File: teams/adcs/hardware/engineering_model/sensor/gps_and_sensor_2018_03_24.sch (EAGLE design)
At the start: 50 parts, among them U1 LT1761-X, U2 LT1761-X, U3 OEM719, U4 LTC3624

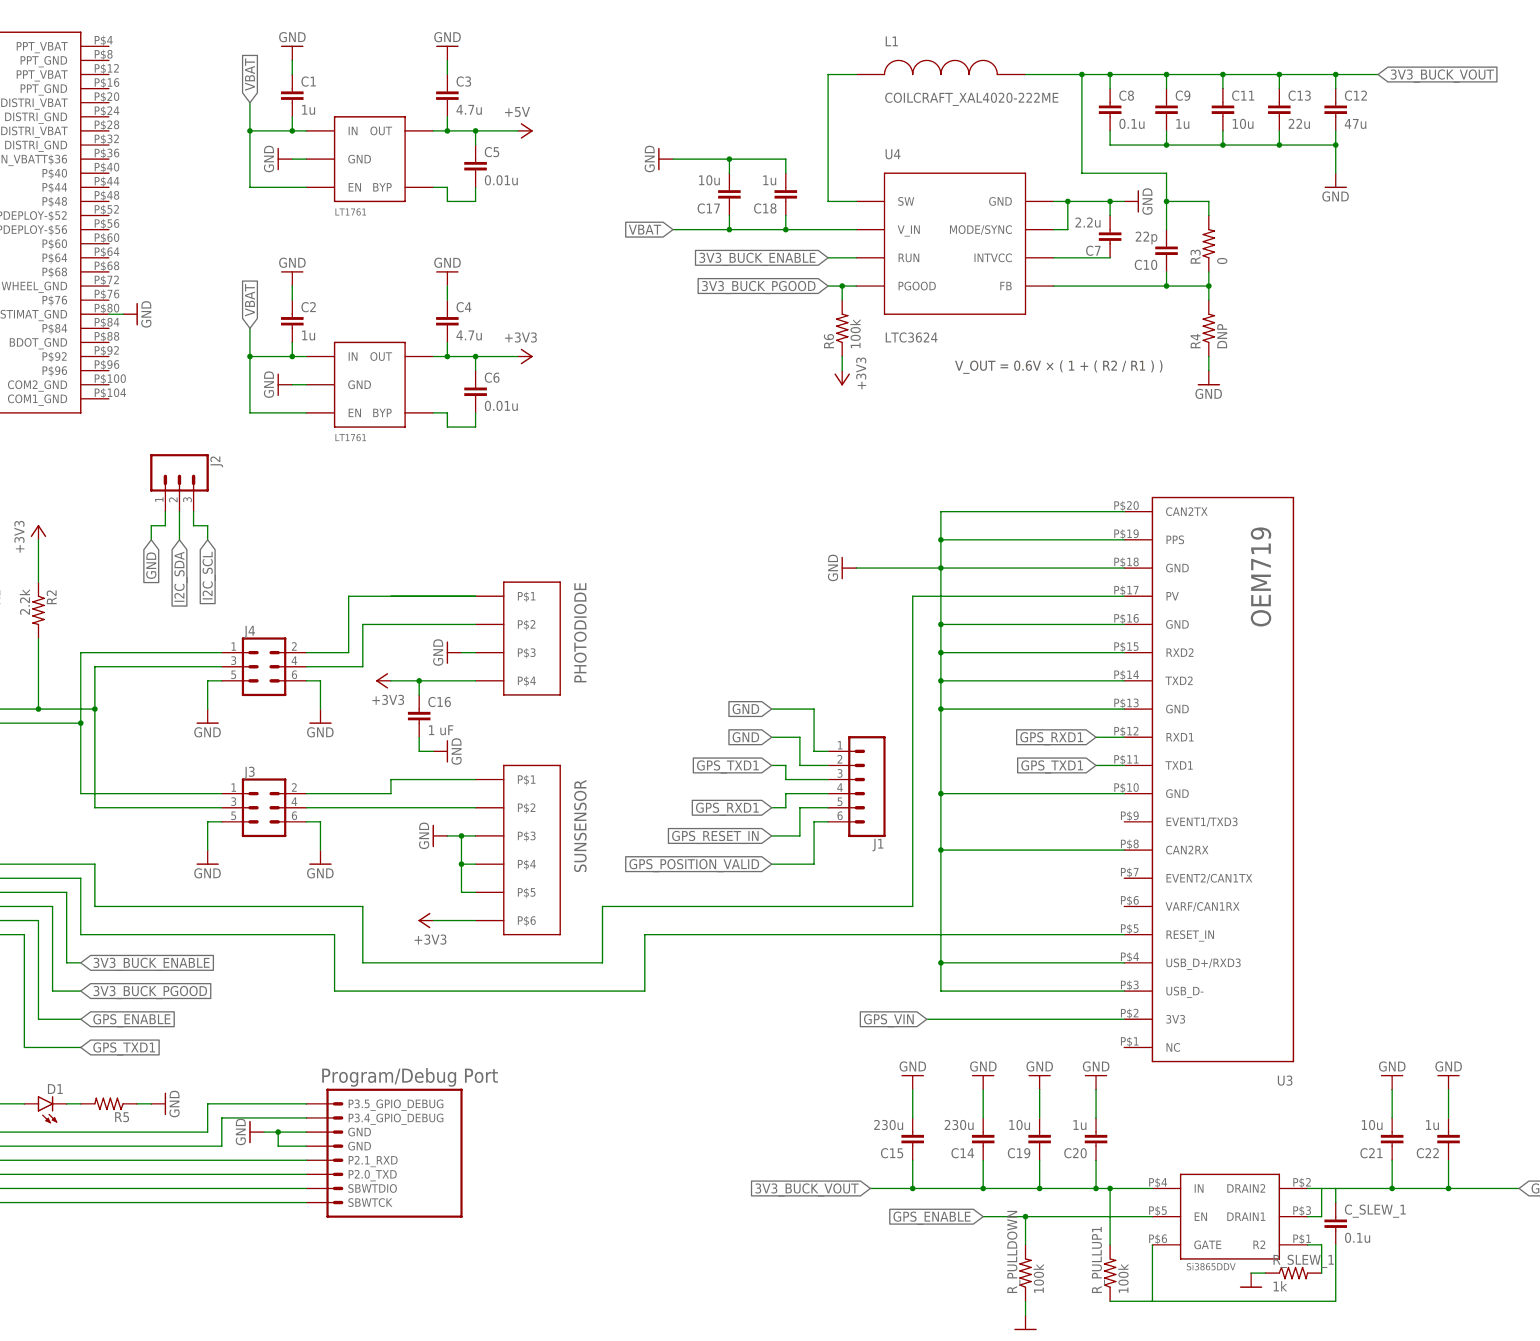
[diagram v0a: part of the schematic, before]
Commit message: ADCS/Sensor: Use picolock with more connectors and reformat component values
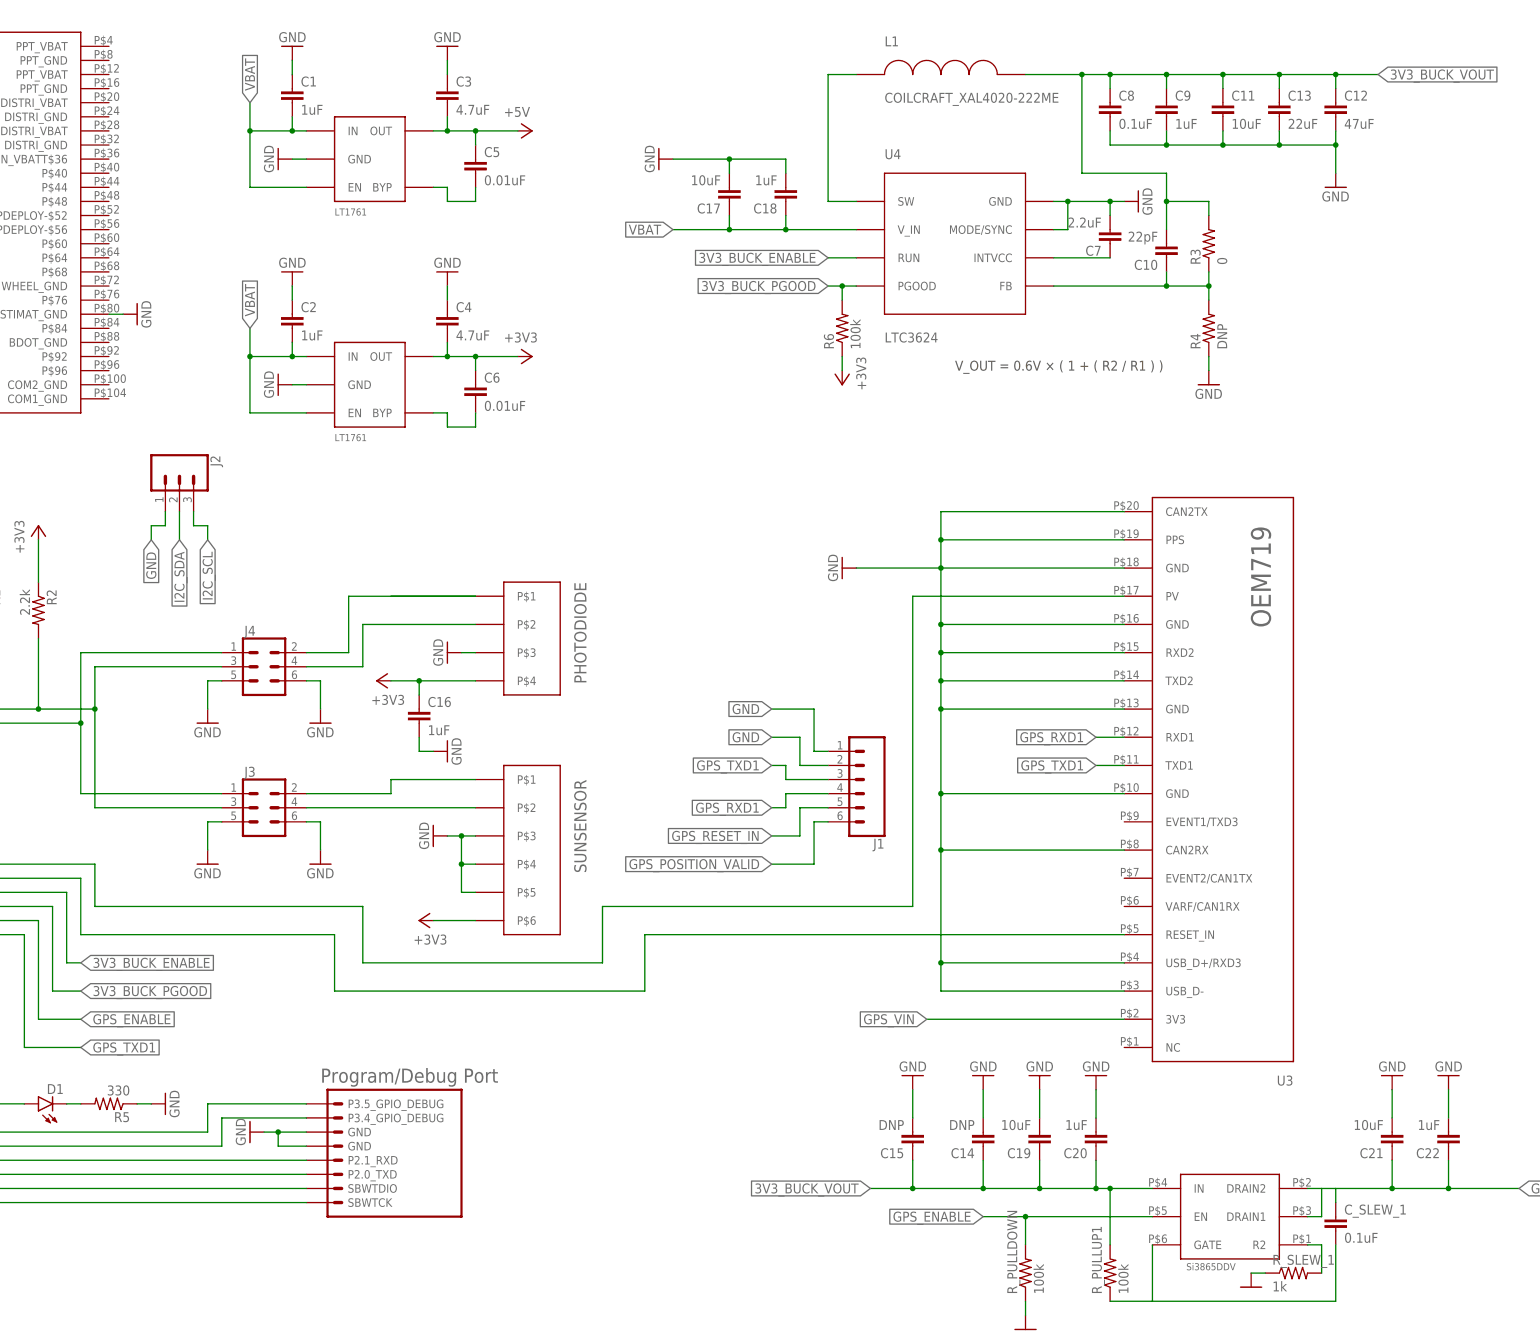
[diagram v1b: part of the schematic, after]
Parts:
- C1, C18, C2, C20, C22, C9: value 1u -> 1uF
- C10: value 22p -> 22pF
- C11, C17, C19, C21: value 10u -> 10uF
- C12: value 47u -> 47uF
- C13: value 22u -> 22uF
- C14, C15: value 230u -> DNP
- C16: value 1 uF -> 1uF
- C3, C4: value 4.7u -> 4.7uF
- C5, C6: value 0.01u -> 0.01uF
- C7: value 2.2u -> 2.2uF
- C8, C_SLEW_1: value 0.1u -> 0.1uF
- R5: value (none) -> 330
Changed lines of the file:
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@@
 <part name="GND7" library="supply1" library_urn="urn:adsk.eagle:library:371" deviceset="GND" device=""/>
 <part name="P+2" library="supply1" library_urn="urn:adsk.eagle:library:371" deviceset="+5V" device=""/>
-<part name="C5" library="DubSat1 Components" deviceset="CAPACITOR" device="0805" value="0.01u"/>
-<part name="C1" library="DubSat1 Components" deviceset="CAPACITOR" device="0805" value="1u"/>
+<part name="C5" library="DubSat1 Components" deviceset="CAPACITOR" device="0805" value="0.01uF"/>
+<part name="C1" library="DubSat1 Components" deviceset="CAPACITOR" device="0805" value="1uF"/>
 <part name="GND9" library="supply1" library_urn="urn:adsk.eagle:library:371" deviceset="GND" device=""/>
-<part name="C3" library="DubSat1 Components" deviceset="CAPACITOR" device="0805" value="4.7u"/>
+<part name="C3" library="DubSat1 Components" deviceset="CAPACITOR" device="0805" value="4.7uF"/>
 <part name="GND11" library="supply1" library_urn="urn:adsk.eagle:library:371" deviceset="GND" device=""/>
 <part name="U2" library="DubSat1 Components" deviceset="LT1761-X" device=""/>
 <part name="GND8" library="supply1" library_urn="urn:adsk.eagle:library:371" deviceset="GND" device=""/>
 <part name="+3V36" library="supply1" library_urn="urn:adsk.eagle:library:371" deviceset="+3V3" device=""/>
-<part name="C6" library="DubSat1 Components" deviceset="CAPACITOR" device="0805" value="0.01u"/>
-<part name="C2" library="DubSat1 Components" deviceset="CAPACITOR" device="0805" value="1u"/>
+<part name="C6" library="DubSat1 Components" deviceset="CAPACITOR" device="0805" value="0.01uF"/>
+<part name="C2" library="DubSat1 Components" deviceset="CAPACITOR" device="0805" value="1uF"/>
 <part name="GND10" library="supply1" library_urn="urn:adsk.eagle:library:371" deviceset="GND" device=""/>
-<part name="C4" library="DubSat1 Components" deviceset="CAPACITOR" device="0805" value="4.7u"/>
+<part name="C4" library="DubSat1 Components" deviceset="CAPACITOR" device="0805" value="4.7uF"/>
 <part name="GND12" library="supply1" library_urn="urn:adsk.eagle:library:371" deviceset="GND" device=""/>
 <part name="PHOTODIODE" library="DubSat1 Components" deviceset="PICOLOCK_4" device=""/>
@@
 <part name="U4" library="DubSat1 Components" deviceset="LTC3624" device=""/>
 <part name="GND13" library="supply1" library_urn="urn:adsk.eagle:library:371" deviceset="GND" device=""/>
-<part name="C7" library="DubSat1 Components" deviceset="CAPACITOR" device="0805" value="2.2u"/>
+<part name="C7" library="DubSat1 Components" deviceset="CAPACITOR" device="0805" value="2.2uF"/>
 <part name="L1" library="DubSat1 Components" deviceset="COILCRAFT_XAL4020-222ME" device=""/>
 <part name="GND14" library="supply1" library_urn="urn:adsk.eagle:library:371" deviceset="GND" device=""/>
 <part name="R3" library="DubSat1 Components" deviceset="RESISTOR" device="0805" value="0"/>
 <part name="R4" library="DubSat1 Components" deviceset="RESISTOR" device="0805" value="DNP"/>
-<part name="C10" library="DubSat1 Components" deviceset="CAPACITOR" device="0805" value="22p"/>
-<part name="C8" library="DubSat1 Components" deviceset="CAPACITOR" device="0805" value="0.1u"/>
-<part name="C9" library="DubSat1 Components" deviceset="CAPACITOR" device="0805" value="1u"/>
-<part name="C11" library="DubSat1 Components" deviceset="CAPACITOR" device="0805" value="10u"/>
-<part name="C12" library="DubSat1 Components" deviceset="CAPACITOR" device="1206" value="47u"/>
+<part name="C10" library="DubSat1 Components" deviceset="CAPACITOR" device="0805" value="22pF"/>
+<part name="C8" library="DubSat1 Components" deviceset="CAPACITOR" device="0805" value="0.1uF"/>
+<part name="C9" library="DubSat1 Components" deviceset="CAPACITOR" device="0805" value="1uF"/>
+<part name="C11" library="DubSat1 Components" deviceset="CAPACITOR" device="0805" value="10uF"/>
+<part name="C12" library="DubSat1 Components" deviceset="CAPACITOR" device="1206" value="47uF"/>
 <part name="GND15" library="supply1" library_urn="urn:adsk.eagle:library:371" deviceset="GND" device=""/>
 <part name="U$1" library="HuskySat-1 Logos" deviceset="LOGO_MOLEX" device=""/>
 <part name="U$3" library="DubSat1 Components" deviceset="SI3865DDV" device=""/>
-<part name="C_SLEW_1" library="DubSat1 Components" deviceset="CAPACITOR" device="0805" value="0.1u"/>
+<part name="C_SLEW_1" library="DubSat1 Components" deviceset="CAPACITOR" device="0805" value="0.1uF"/>
 <part name="R_SLEW_1" library="DubSat1 Components" deviceset="RESISTOR" device="0805" value="1k"/>
 <part name="GND17" library="SparkFun-Aesthetics" deviceset="DGND" device=""/>
 <part name="R_PULLUP1" library="DubSat1 Components" deviceset="RESISTOR" device="0805" value="100k"/>
-<part name="C14" library="DubSat1 Components" deviceset="CAPACITOR" device="PANASONIC_16SVPG270M" value="230u"/>
-<part name="C15" library="DubSat1 Components" deviceset="CAPACITOR" device="PANASONIC_16SVPG270M" value="230u"/>
+<part name="C14" library="DubSat1 Components" deviceset="CAPACITOR" device="PANASONIC_16SVPG270M" value="DNP"/>
+<part name="C15" library="DubSat1 Components" deviceset="CAPACITOR" device="PANASONIC_16SVPG270M" value="DNP"/>
 <part name="GND18" library="supply1" library_urn="urn:adsk.eagle:library:371" deviceset="GND" device=""/>
 <part name="GND19" library="supply1" library_urn="urn:adsk.eagle:library:371" deviceset="GND" device=""/>
-<part name="C13" library="DubSat1 Components" deviceset="CAPACITOR" device="1206" value="22u"/>
+<part name="C13" library="DubSat1 Components" deviceset="CAPACITOR" device="1206" value="22uF"/>
 <part name="U$2" library="DubSat1 Components" deviceset="PROGRAM/DEBUG_PORT" device=""/>
 <part name="GND16" library="supply1" library_urn="urn:adsk.eagle:library:371" deviceset="GND" device=""/>
 <part name="D1" library="DubSat1 Components" deviceset="LED" device=""/>
-<part name="R5" library="DubSat1 Components" deviceset="RESISTOR" device="0805"/>
+<part name="R5" library="DubSat1 Components" deviceset="RESISTOR" device="0805" value="330"/>
 <part name="GND20" library="supply1" library_urn="urn:adsk.eagle:library:371" deviceset="GND" device=""/>
 <part name="J1" library="SparkFun-Connectors" deviceset="CONN_06" device="LOCK"/>
@@
 <part name="GND23" library="supply1" library_urn="urn:adsk.eagle:library:371" deviceset="GND" device=""/>
 <part name="GND24" library="supply1" library_urn="urn:adsk.eagle:library:371" deviceset="GND" device=""/>
-<part name="C16" library="DubSat1 Components" deviceset="CAPACITOR" device="0805" value="1 uF"/>
+<part name="C16" library="DubSat1 Components" deviceset="CAPACITOR" device="0805" value="1uF"/>
 <part name="GND25" library="supply1" library_urn="urn:adsk.eagle:library:371" deviceset="GND" device=""/>
-<part name="C17" library="DubSat1 Components" deviceset="CAPACITOR" device="0805" value="10u"/>
-<part name="C18" library="DubSat1 Components" deviceset="CAPACITOR" device="0805" value="1u"/>
+<part name="C17" library="DubSat1 Components" deviceset="CAPACITOR" device="0805" value="10uF"/>
+<part name="C18" library="DubSat1 Components" deviceset="CAPACITOR" device="0805" value="1uF"/>
 <part name="GND26" library="supply1" library_urn="urn:adsk.eagle:library:371" deviceset="GND" device=""/>
-<part name="C19" library="DubSat1 Components" deviceset="CAPACITOR" device="0805" value="10u"/>
+<part name="C19" library="DubSat1 Components" deviceset="CAPACITOR" device="0805" value="10uF"/>
 <part name="GND27" library="supply1" library_urn="urn:adsk.eagle:library:371" deviceset="GND" device=""/>
-<part name="C20" library="DubSat1 Components" deviceset="CAPACITOR" device="0805" value="1u"/>
+<part name="C20" library="DubSat1 Components" deviceset="CAPACITOR" device="0805" value="1uF"/>
 <part name="GND28" library="supply1" library_urn="urn:adsk.eagle:library:371" deviceset="GND" device=""/>
-<part name="C21" library="DubSat1 Components" deviceset="CAPACITOR" device="0805" value="10u"/>
+<part name="C21" library="DubSat1 Components" deviceset="CAPACITOR" device="0805" value="10uF"/>
 <part name="GND29" library="supply1" library_urn="urn:adsk.eagle:library:371" deviceset="GND" device=""/>
-<part name="C22" library="DubSat1 Components" deviceset="CAPACITOR" device="0805" value="1u"/>
+<part name="C22" library="DubSat1 Components" deviceset="CAPACITOR" device="0805" value="1uF"/>
 <part name="GND30" library="supply1" library_urn="urn:adsk.eagle:library:371" deviceset="GND" device=""/>
 <part name="R_PULLDOWN" library="DubSat1 Components" deviceset="RESISTOR" device="0805" value="100k"/>
